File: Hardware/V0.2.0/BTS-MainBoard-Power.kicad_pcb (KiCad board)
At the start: 4 copper layers, 0 parts

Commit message: Started first routing steps
Signed-off-by: bebenlebricolo <benoittarrade@hotmail.fr>
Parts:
- added C1: 1uF, Capacitor_SMD:C_1206_3216Metric_Pad1.33x1.80mm_HandSolder, F.Cu at (237.5, 87.8)
- added C10: 22nF, Capacitor_SMD:C_1210_3225Metric_Pad1.33x2.70mm_HandSolder, F.Cu at (48.9, 85.5)
- added C11: 1uF, Capacitor_SMD:C_1206_3216Metric_Pad1.33x1.80mm_HandSolder, F.Cu at (138.0, 117.0)
- added C12: 100nF, Capacitor_SMD:C_1206_3216Metric_Pad1.33x1.80mm_HandSolder, F.Cu at (135.5, 117.0)
- added C2: 1uF, Capacitor_SMD:C_1206_3216Metric_Pad1.33x1.80mm_HandSolder, F.Cu at (247.2, 77.3)
- added C3: 470uF, Capacitor_SMD:CP_Elec_10x10, F.Cu at (180.2, 46.0)
- added C4: 470uF, Capacitor_SMD:CP_Elec_10x10, F.Cu at (167.0, 45.5)
- added C5: 470uF, Capacitor_SMD:CP_Elec_10x10, F.Cu at (180.8, 57.5)
- added C6: 100nF, Capacitor_SMD:C_1206_3216Metric_Pad1.33x1.80mm_HandSolder, F.Cu at (181.5, 86.8)
- added C7: 100nF, Capacitor_SMD:C_1206_3216Metric_Pad1.33x1.80mm_HandSolder, F.Cu at (181.5, 76.8)
- added C8: 1uF, Capacitor_SMD:C_1206_3216Metric_Pad1.33x1.80mm_HandSolder, F.Cu at (181.5, 89.2)
- added C9: 100nF, Capacitor_SMD:C_1206_3216Metric_Pad1.33x1.80mm_HandSolder, F.Cu at (125.2, 117.2)
- added D1: SS56B, BTS-MainBoard-Power:SS56B, F.Cu at (173.2, 77.8)
- added D2: SS56B, BTS-MainBoard-Power:SS56B, F.Cu at (126.2, 124.8)
- added D3: 1N4148W, Diode_SMD:D_SOD-123, F.Cu at (253.8, 113.8)
- added H1: MountingHole_Pad, MountingHole:MountingHole_4mm_Pad_Via, F.Cu at (192.5, 126.5)
- added H2: MountingHole_Pad, MountingHole:MountingHole_4mm_Pad_Via, F.Cu at (105.5, 43.5)
- added H3: MountingHole_Pad, MountingHole:MountingHole_4mm_Pad_Via, F.Cu at (192.2, 44.0)
- added H4: MountingHole_Pad, MountingHole:MountingHole_4mm_Pad_Via, F.Cu at (101.5, 126.8)
- added H5: MountingHole_Pad, MountingHole:MountingHole_3mm_Pad_Via, F.Cu at (148.8, 44.5)
- added H6: MountingHole_Pad, MountingHole:MountingHole_3mm_Pad_Via, F.Cu at (155.5, 44.5)
- added H7: MountingHole_Pad, MountingHole:MountingHole_3mm_Pad_Via, F.Cu at (138.6, 44.5)
- added H8: MountingHole_Pad, MountingHole:MountingHole_3mm_Pad_Via, F.Cu at (131.8, 44.5)
- added J10: PeCon, BTS-MainBoard-Power:TE_1-1123723-2_1x02_P3.96mm_8Amps_Vertical, F.Cu at (115.5, 97.4)
- added J11: PeCon, BTS-MainBoard-Power:TE_1-1123723-2_1x02_P3.96mm_8Amps_Vertical, F.Cu at (105.2, 66.7)
- added J12: FanConn, Connector_PinSocket_2.54mm:PinSocket_1x02_P2.54mm_Vertical, F.Cu at (186.5, 105.0)
- added J13: FanConn, Connector_PinSocket_2.54mm:PinSocket_1x02_P2.54mm_Vertical, F.Cu at (191.3, 105.0)
- added J14: FanConn, Connector_PinSocket_2.54mm:PinSocket_1x02_P2.54mm_Vertical, F.Cu at (176.5, 105.0)
- added J15: FanConn, Connector_PinSocket_2.54mm:PinSocket_1x02_P2.54mm_Vertical, F.Cu at (181.6, 112.2)
- added J16: FanConn, Connector_PinSocket_2.54mm:PinSocket_1x02_P2.54mm_Vertical, F.Cu at (176.6, 112.2)
- added J17: FanConn, Connector_PinSocket_2.54mm:PinSocket_1x02_P2.54mm_Vertical, F.Cu at (186.5, 112.2)
- added J18: FanConn, Connector_PinSocket_2.54mm:PinSocket_1x02_P2.54mm_Vertical, F.Cu at (191.3, 112.5)
- added J19: FanConn, Connector_PinSocket_2.54mm:PinSocket_1x02_P2.54mm_Vertical, F.Cu at (181.6, 105.0)
- added J3: LogicBoardConnector, Connector_PinHeader_2.54mm:PinHeader_1x07_P2.54mm_Vertical, F.Cu at (192.3, 80.2)
- added J4: PeCon, BTS-MainBoard-Power:TE_1-1123723-2_1x02_P3.96mm_8Amps_Vertical, F.Cu at (115.2, 66.7)
- added J5: PeCon, BTS-MainBoard-Power:TE_1-1123723-2_1x02_P3.96mm_8Amps_Vertical, F.Cu at (105.8, 97.5)
- added J6: PeCon, BTS-MainBoard-Power:TE_1-1123723-2_1x02_P3.96mm_8Amps_Vertical, F.Cu at (105.5, 87.4)
- added J7: PeCon, BTS-MainBoard-Power:TE_1-1123723-2_1x02_P3.96mm_8Amps_Vertical, F.Cu at (115.5, 77.2)
- added J8: PeCon, BTS-MainBoard-Power:TE_1-1123723-2_1x02_P3.96mm_8Amps_Vertical, F.Cu at (115.5, 87.4)
- added J9: PeCon, BTS-MainBoard-Power:TE_1-1123723-2_1x02_P3.96mm_8Amps_Vertical, F.Cu at (105.5, 77.2)
- added L1: SRP1270-100M, BTS-MainBoard-Power:L_Bourns_SRP1270, F.Cu at (149.2, 91.5)
- added L2: SRP1270-100M, BTS-MainBoard-Power:L_Bourns_SRP1270, F.Cu at (149.2, 76.0)
- added L3: SRP1270-100M, BTS-MainBoard-Power:L_Bourns_SRP1270, F.Cu at (133.2, 91.5)
- added L4: SRP1270-100M, BTS-MainBoard-Power:L_Bourns_SRP1270, F.Cu at (133.2, 75.8)
- added Q1: DMG3418L, Package_TO_SOT_SMD:SOT-23, F.Cu at (257.0, 70.8)
- added Q2: NTMFS5H419NL, BTS-MainBoard-Power:NTMFS5G419NL, F.Cu at (166.5, 77.2)
- added Q3: NTMFS5H419NL, BTS-MainBoard-Power:NTMFS5G419NL, F.Cu at (166.5, 86.0)
- added Q4: NTMFS5H419NL, BTS-MainBoard-Power:NTMFS5G419NL, F.Cu at (199.0, 105.5)
- added Q5: NTMFS5H419NL, BTS-MainBoard-Power:NTMFS5G419NL, F.Cu at (199.0, 113.2)
- added R1: 3.3, Resistor_SMD:R_1206_3216Metric_Pad1.30x1.75mm_HandSolder, F.Cu at (177.2, 81.5)
- added R10: 220, Resistor_SMD:R_1206_3216Metric_Pad1.30x1.75mm_HandSolder, F.Cu at (187.8, 85.0)
- added R11: 220, Resistor_SMD:R_1206_3216Metric_Pad1.30x1.75mm_HandSolder, F.Cu at (134.0, 113.0)
- added R12: 220, Resistor_SMD:R_1206_3216Metric_Pad1.30x1.75mm_HandSolder, F.Cu at (134.0, 110.5)
- added R2: 1k, Resistor_SMD:R_1206_3216Metric_Pad1.30x1.75mm_HandSolder, F.Cu at (235.3, 91.6)
- added R3: 3.3, Resistor_SMD:R_1206_3216Metric_Pad1.30x1.75mm_HandSolder, F.Cu at (130.5, 121.0)
- added R4: 3.3, Resistor_SMD:R_1206_3216Metric_Pad1.30x1.75mm_HandSolder, F.Cu at (180.0, 74.2)
- added R5: 3.3, Resistor_SMD:R_1206_3216Metric_Pad1.30x1.75mm_HandSolder, F.Cu at (185.8, 79.2)
- added R6: 0.01, Resistor_SMD:R_2512_6332Metric_Pad1.40x3.35mm_HandSolder, F.Cu at (179.8, 127.5)
- added R7: 3.3, Resistor_SMD:R_1206_3216Metric_Pad1.30x1.75mm_HandSolder, F.Cu at (122.8, 118.8)
- added R8: 3.3, Resistor_SMD:R_1206_3216Metric_Pad1.30x1.75mm_HandSolder, F.Cu at (126.2, 113.0)
- added R9: 220, Resistor_SMD:R_1206_3216Metric_Pad1.30x1.75mm_HandSolder, F.Cu at (185.5, 85.0)
- added U1: LM5109BMA, Package_SO:SOIC-8_3.9x4.9mm_P1.27mm, F.Cu at (181.5, 81.8)
- added U2: LM5109BMA, Package_SO:SOIC-8_3.9x4.9mm_P1.27mm, F.Cu at (130.2, 117.0)
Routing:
- net /BHO_Sig: track 0.00 -> 17.0 mm
- net /HBridge/AHO_Gate: track 0.00 -> 15.1 mm
- net /AHO_Sig: track 0.00 -> 13.9 mm
- net /ALO_Sig: track 0.00 -> 12.6 mm
- net /BLO_Sig: track 0.00 -> 11.7 mm
- net GND: track 0.00 -> 5.53 mm, vias 0 -> 4
- net /AHO: track 0.00 -> 5.31 mm
- net /AHS: track 0.00 -> 3.04 mm
- net /ALO: track 0.00 -> 3.03 mm
- net /Psu12V: track 0.00 -> 2.88 mm, vias 0 -> 2
- net /HBridge/BLO_Gate: track 0.00 -> 1.10 mm, vias 0 -> 1
- added copper zone on F.Cu, net /AHS
- added copper zone on F.Cu, net /BHS
- added copper zone on F.Cu, net /DBootAnode1
- added copper zone on F.Cu, net /DBootAnode2
- added copper zone on F.Cu, net /HBoot1
- added copper zone on F.Cu, net /HBoot2
- added copper zone on F.Cu, net /HBridge/+Peltier
- added copper zone on F.Cu, net /Psu12V
- added copper zone on In2.Cu, net /Psu12V
- added copper zone on F.Cu, net /VSense
- added copper zone on F.Cu, net GND
- added copper zone on In1.Cu, net GND
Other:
- board outline added: 100 x 100 mm
- board text added: "Logic board avr bounding area"
- board text added: "MCU"

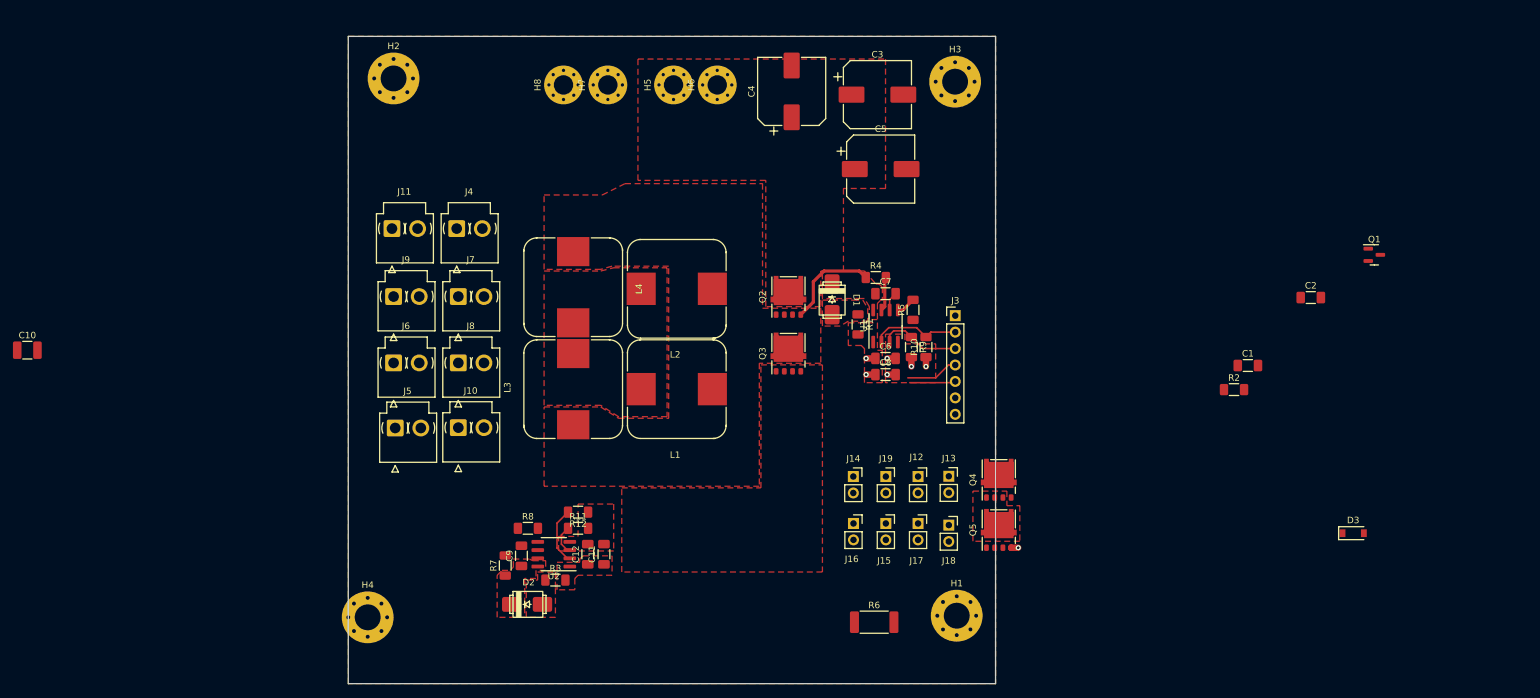
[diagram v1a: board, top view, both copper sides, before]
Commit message: Improved zoning thermal layout
Signed-off-by: bebenlebricolo <benoittarrade@hotmail.fr>
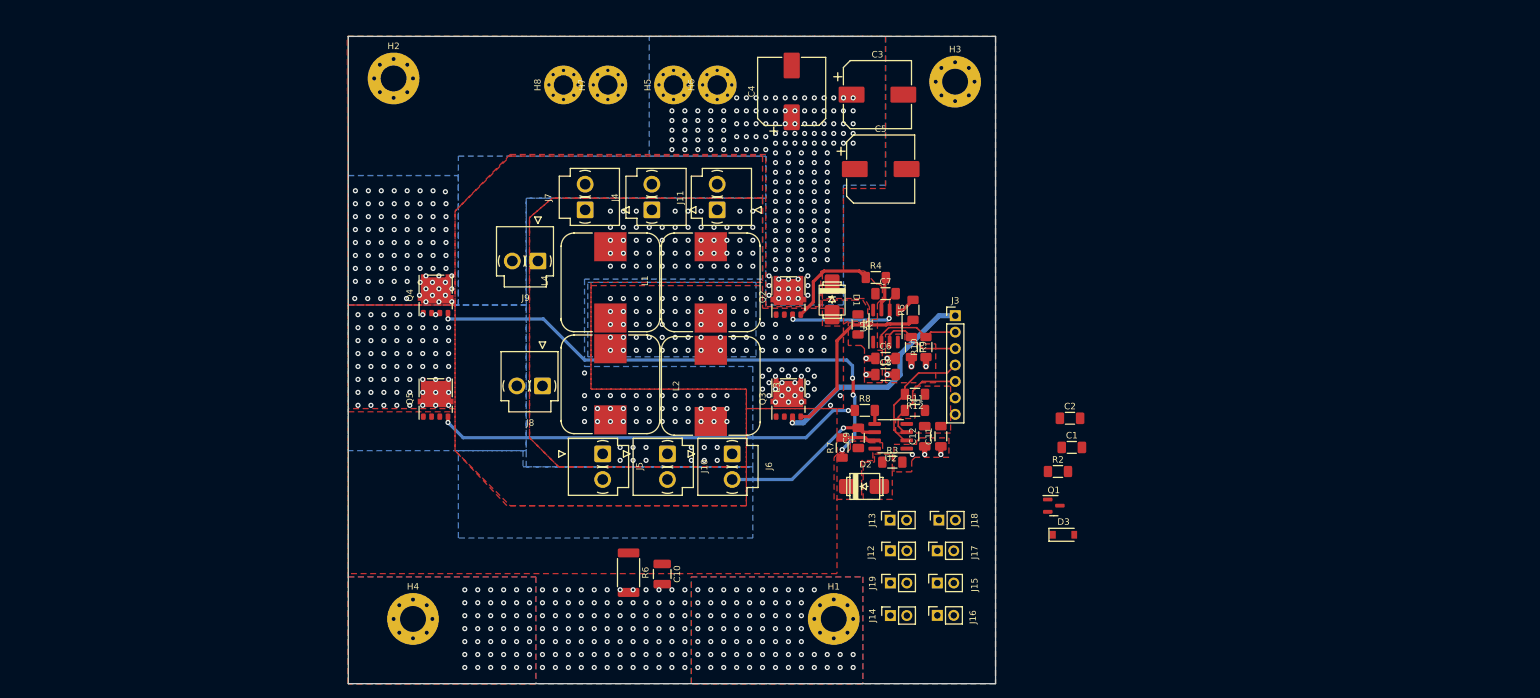
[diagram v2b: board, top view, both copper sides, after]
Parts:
- moved C10 104.0 mm to (147.0, 120.1), turned to -90 degrees
- moved Q4 91.5 mm to (112.0, 77.0)
- moved Q5 89.3 mm to (112.0, 93.0)
- moved Q1 62.9 mm to (207.5, 109.5)
- moved C11 55.1 mm to (190.1, 98.8)
- moved C12 55.1 mm to (187.6, 98.8)
- moved C9 55.1 mm to (177.3, 99.0)
- moved D2 55.1 mm to (178.3, 106.5)
- moved R11 55.1 mm to (186.1, 94.8)
- moved R12 55.1 mm to (186.1, 92.3)
- moved R3 55.1 mm to (182.6, 102.8)
- moved R7 55.1 mm to (174.8, 100.5)
- moved R8 55.1 mm to (178.3, 94.8)
- moved U2 55.1 mm to (182.3, 98.8)
- moved J6 54.2 mm to (157.8, 101.5), turned to -90 degrees
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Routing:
- net /HBridge/BHO_Gate: track 0.00 -> 81.5 mm, vias 0 -> 4
- net /HBridge/BLO_Gate: track 1.10 -> 66.5 mm, vias 1 -> 2
- net /VSense: track 0.00 -> 34.8 mm, vias 0 -> 1
- net /HBridge/ALO_Gate: track 0.00 -> 27.9 mm
- net /BHS: track 0.00 -> 25.6 mm, vias 0 -> 106
- net /AHS: track 3.04 -> 20.0 mm, vias 0 -> 168
- net /BHO: track 0.00 -> 5.21 mm
- net /BLO_Sig: track 11.7 -> 15.2 mm
- net /Psu12V: track 2.88 -> 5.39 mm, vias 2 -> 254
- net /BHO_Sig: track 17.0 -> 19.2 mm
- net /BLO: track 0.00 -> 2.11 mm
- net GND: vias 4 -> 90
- net /HBridge/+Peltier: vias 0 -> 105
- added copper zone on B.Cu, net /AHS
- added copper zone on In2.Cu, net /AHS
- added copper zone on B.Cu, net /BHS
- added copper zone on In2.Cu, net /BHS
- added copper zone on B.Cu, net /HBridge/+Peltier
- added copper zone on B.Cu, net /Psu12V
- added copper zone on B.Cu, net GND

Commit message: Rewired the whole PCB with much more compact design
Signed-off-by: bebenlebricolo <benoittarrade@hotmail.fr>
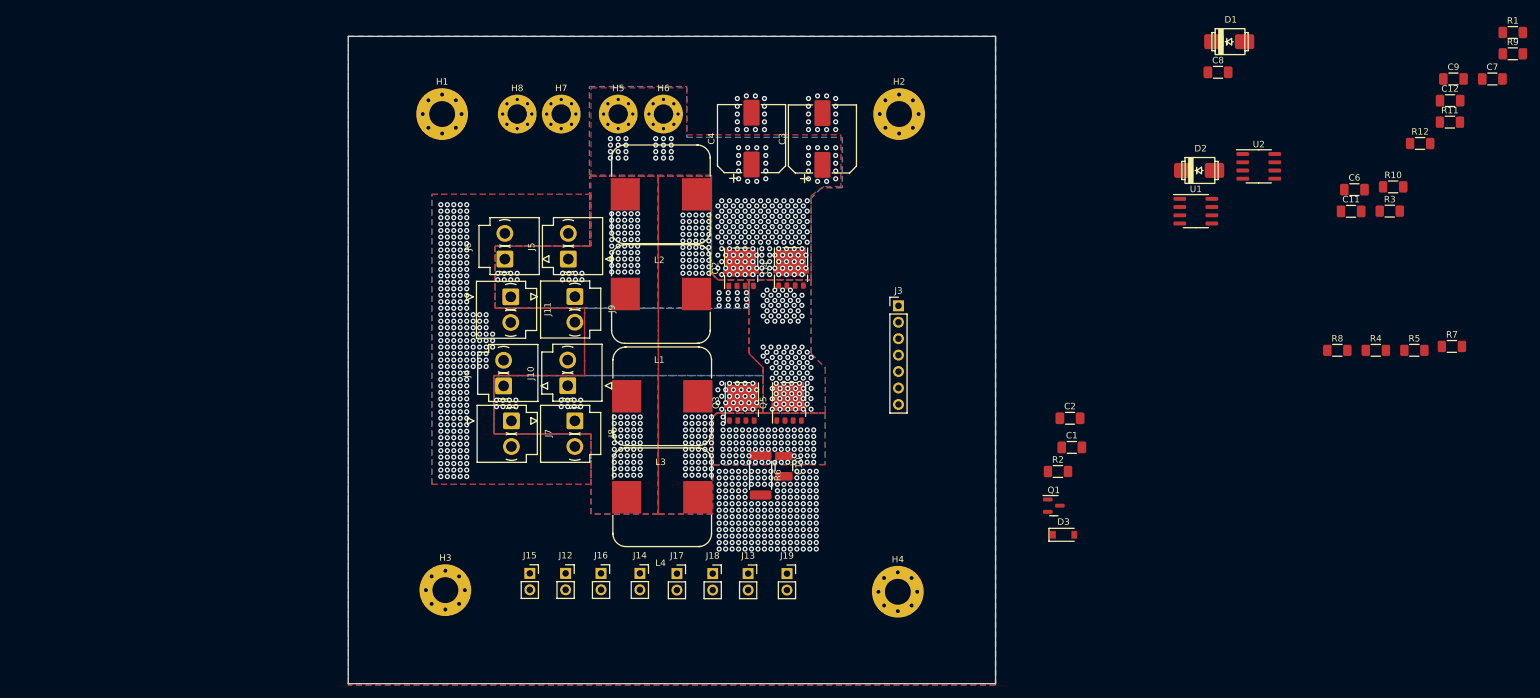
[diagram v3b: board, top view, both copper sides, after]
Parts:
- removed C5: 470uF, Capacitor_SMD:CP_Elec_10x10
- moved H3 111.2 mm to (113.5, 122.5)
- moved R1 110.8 mm to (278.4, 36.4), turned to 0 degrees
- moved C9 107.4 mm to (269.2, 43.6), turned to 0 degrees
- moved R9 103.4 mm to (278.4, 39.7), turned to 0 degrees
- moved C7 99.4 mm to (275.2, 43.6)
- moved H1 98.7 mm to (113.0, 49.0)
- moved C12 96.3 mm to (268.7, 46.9), turned to 0 degrees
- moved R7 95.5 mm to (269.0, 84.9), turned to 0 degrees
- moved R11 93.9 mm to (268.7, 50.2)
- moved R12 87.1 mm to (264.1, 53.5), turned to 0 degrees
- moved R3 86.1 mm to (259.4, 64.0)
- moved H2 78.3 mm to (183.6, 49.0)
- moved R4 78.1 mm to (257.2, 85.5)
- moved R5 77.7 mm to (263.2, 85.5), turned to 0 degrees
- moved C6 77.0 mm to (253.9, 60.7)
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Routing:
- net /HBridge/BHO_Gate: track 81.5 -> 0.00 mm, vias 4 -> 0
- net /HBridge/BLO_Gate: track 66.5 -> 0.00 mm, vias 2 -> 0
- net /VSense: track 34.8 -> 0.00 mm, vias 1 -> 86
- net /HBridge/ALO_Gate: track 27.9 -> 0.00 mm
- net /BHS: track 25.6 -> 0.00 mm, vias 106 -> 357
- net /AHS: track 20.0 -> 0.00 mm, vias 168 -> 139
- net /BHO_Sig: track 19.2 -> 0.00 mm
- net /BLO_Sig: track 15.2 -> 0.00 mm
- net /HBridge/AHO_Gate: track 15.1 -> 0.00 mm
- net /AHO_Sig: track 13.9 -> 0.00 mm
- net /ALO_Sig: track 12.6 -> 0.00 mm
- net GND: track 5.53 -> 0.00 mm, vias 90 -> 222
- net /Psu12V: track 5.39 -> 0.00 mm, vias 254 -> 219
- net /AHO: track 5.31 -> 0.00 mm
- net /BHO: track 5.21 -> 0.00 mm
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- added copper zone on B.Cu, net /VSense
- removed copper zone on In2.Cu, net /AHS
- removed copper zone on F.Cu, net /DBootAnode1
- removed copper zone on F.Cu, net /DBootAnode2
- removed copper zone on F.Cu, net /HBoot1
- removed copper zone on F.Cu, net /HBoot2

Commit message: Finished routing, now needs improvements
Signed-off-by: bebenlebricolo <benoittarrade@hotmail.fr>
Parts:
- moved R1 112.3 mm to (174.3, 78.5), turned to -90 degrees
- moved C9 109.9 mm to (174.6, 99.4), turned to 90 degrees
- moved R9 108.3 mm to (179.3, 83.5), turned to -90 degrees
- moved R11 103.9 mm to (174.6, 94.4), turned to 90 degrees
- moved C7 100.6 mm to (178.8, 72.2)
- moved C12 97.8 mm to (180.5, 89.0), turned to 90 degrees
- moved R12 95.2 mm to (175.7, 89.0), turned to -90 degrees
- moved R7 90.6 mm to (180.0, 101.8), turned to 90 degrees
- moved R3 87.3 mm to (183.4, 107.0), turned to -90 degrees
- moved R10 86.1 mm to (177.0, 83.5), turned to 90 degrees
- moved C6 84.7 mm to (172.3, 83.5), turned to -90 degrees
- moved R5 80.4 mm to (183.5, 74.7), turned to 180 degrees
- moved R4 79.9 mm to (178.9, 69.7)
- moved C11 79.4 mm to (178.1, 89.0), turned to 90 degrees
- moved R8 75.4 mm to (177.7, 101.8), turned to 90 degrees
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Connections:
- D3 pad 1: /Vcc -> /Psu12V
- J12 pad 1: /Vcc -> /Psu12V
- J13 pad 1: /Vcc -> /Psu12V
- J14 pad 1: /Vcc -> /Psu12V
- J15 pad 1: /Vcc -> /Psu12V
- J16 pad 1: /Vcc -> /Psu12V
- J17 pad 1: /Vcc -> /Psu12V
- J18 pad 1: /Vcc -> /Psu12V
- J19 pad 1: /Vcc -> /Psu12V
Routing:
- net /FanSink: track 0.00 -> 57.8 mm
- net /HBridge/ALO_Gate: track 0.00 -> 46.0 mm, vias 0 -> 2
- net /HBridge/BHO_Gate: track 0.00 -> 35.9 mm, vias 0 -> 2
- net /VSense: track 0.00 -> 30.7 mm, vias 86 -> 85
- net /AHS: track 0.00 -> 28.6 mm, vias 139 -> 140
- net /CoolingFanDriveSignal: track 0.00 -> 20.8 mm, vias 0 -> 1
- net /HBridge/AHO_Gate: track 0.00 -> 20.7 mm, vias 0 -> 2
- net /BHO_Sig: track 0.00 -> 15.8 mm, vias 0 -> 1
- net /BLO_Sig: track 0.00 -> 15.6 mm
- net /HBridge/BLO_Gate: track 0.00 -> 13.9 mm
- net /HBoot2: track 0.00 -> 12.4 mm, vias 0 -> 2
- net /AHO_Sig: track 0.00 -> 10.9 mm, vias 0 -> 1
- net /BHS: track 0.00 -> 10.6 mm, vias 357 -> 352
- net /ALO_Sig: track 0.00 -> 7.28 mm
- net /AHO: track 0.00 -> 6.69 mm
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- added copper zone on F.Cu, net /CoolingFanDriveSignal
- added copper zone on F.Cu, net /DBootAnode1
- added copper zone on F.Cu, net /DBootAnode2
- added copper zone on F.Cu, net /FanSink
- added copper zone on F.Cu, net /HBoot1
- added copper zone on F.Cu, net /HBoot2
